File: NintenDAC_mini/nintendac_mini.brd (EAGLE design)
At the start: 26 x 42 mm, 30 parts, among them IC1 STM32F10XCXT6, IC3 24C64ST, X1 USB-MICROB

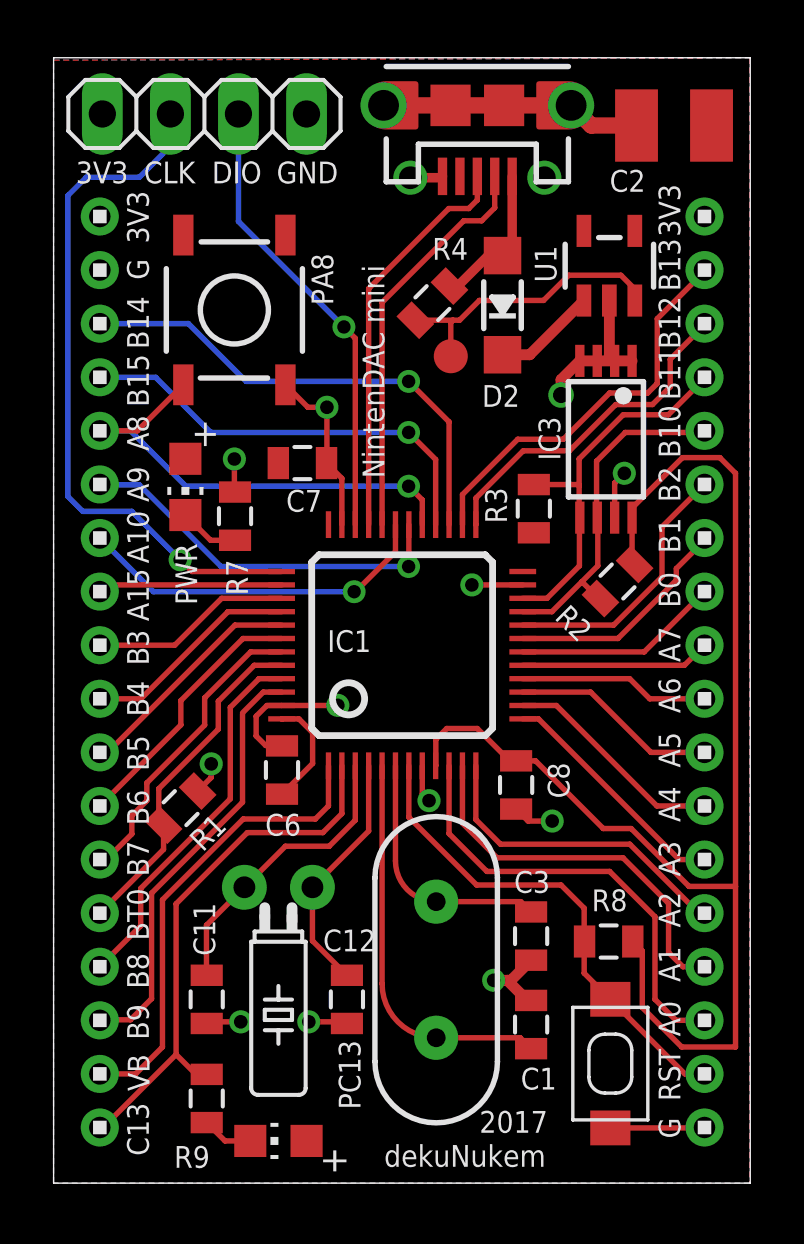
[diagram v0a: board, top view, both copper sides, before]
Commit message: updated power control on mini
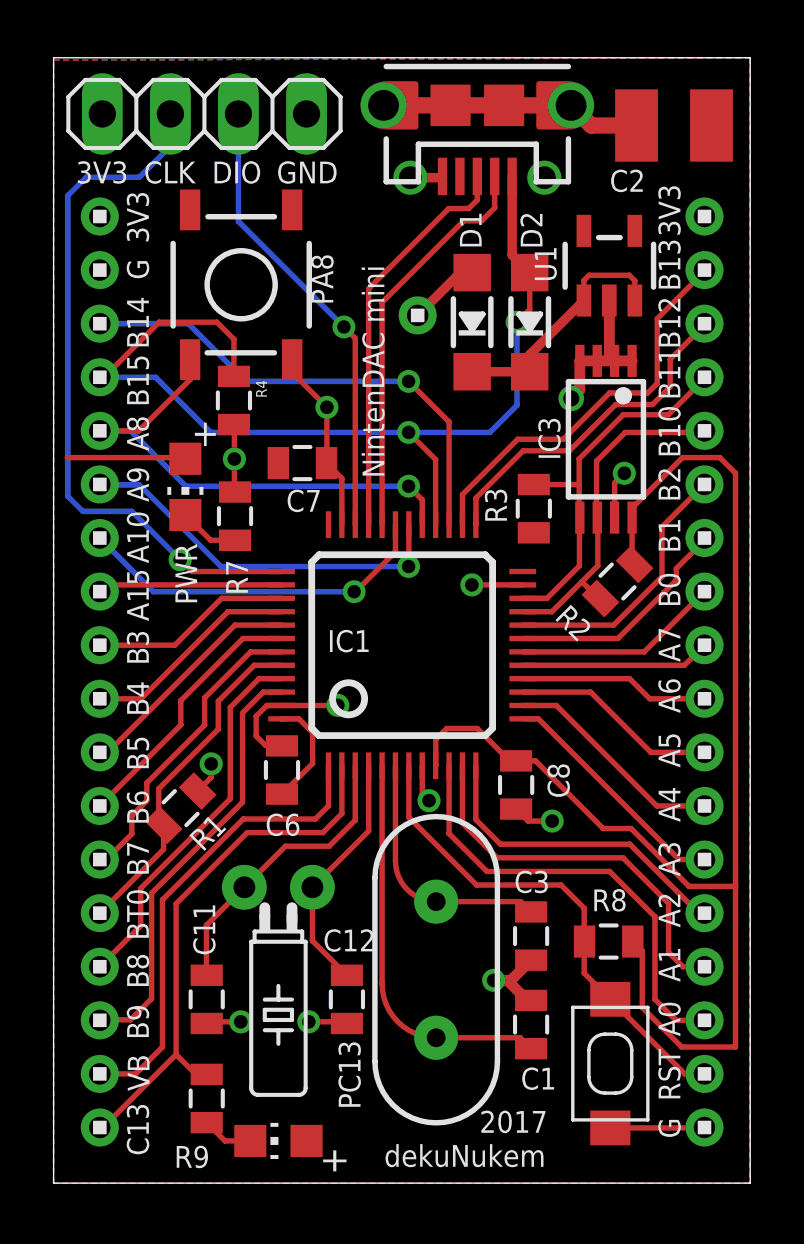
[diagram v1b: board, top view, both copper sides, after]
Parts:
- removed TP1: TEST-POINT3X5, SparkFun-Passives:PAD.03X.05
- added D1: MBR120, microbuilder:SOD-123
- added U$3: 1X1, headers(2mm):1X1
- moved R4 8.25 mm to (6.73, 29.2), turned to 270 degrees
- moved D2 1.20 mm to (17.8, 32.1)
- moved S2 0.97 mm to (7.00, 33.5)
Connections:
- removed net N$2: D2.A, R4.2, X1.VBUS
- net GND: now also R4.2
- net N$31: now also D1.C, U1.3
- net N$36: now also D1.A, U$3.1; no longer R4.1, TP1.P$1, U1.3
- net N$45: now also D2.A, R4.1, X1.VBUS
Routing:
- net N$45: track 16.2 -> 37.2 mm, vias 1 -> 2
- net N$36: track 11.0 -> 2.69 mm
- net N$2: track 5.56 -> 0.00 mm
- net N$31: track 3.88 -> 9.20 mm
- net +3V3: track 54.3 -> 58.7 mm
- net GND: track 46.7 -> 48.4 mm
- net N$43: track 17.9 -> 18.9 mm

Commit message: standby wakeup test
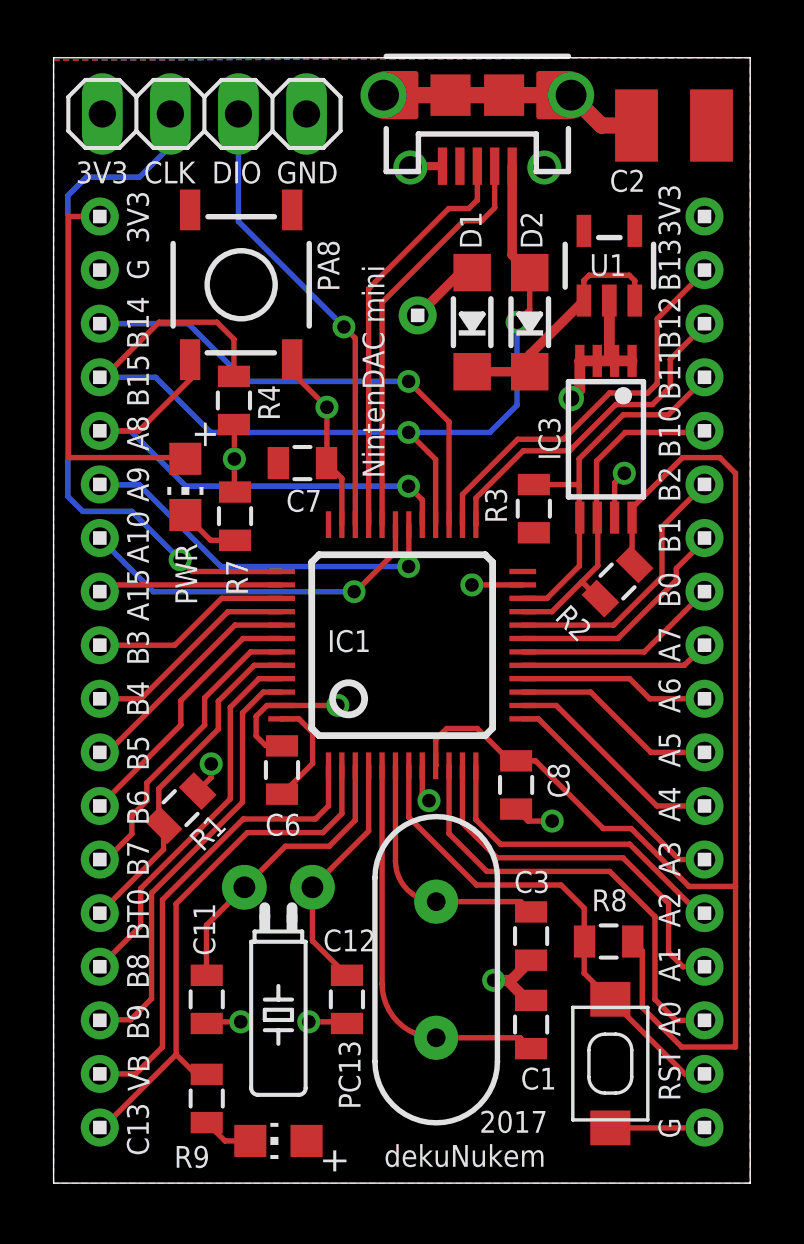
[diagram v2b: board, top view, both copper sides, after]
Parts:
- moved X1 0.38 mm to (15.8, 40.6)
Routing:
- net +3V3: track 58.7 -> 68.7 mm
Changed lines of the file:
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@@
 <setting verticaltext="up"/>
 </settings>
-<grid distance="1" unitdist="mil" unit="mil" style="lines" multiple="1" display="no" altdistance="0.025" altunitdist="inch" altunit="inch"/>
+<grid distance="5" unitdist="mil" unit="mil" style="lines" multiple="1" display="no" altdistance="0.025" altunitdist="inch" altunit="inch"/>
 <layers>
-<layer number="1" name="Top" color="4" fill="1" visible="no" active="yes"/>
+<layer number="1" name="Top" color="4" fill="1" visible="yes" active="yes"/>
 <layer number="16" name="Bottom" color="1" fill="1" visible="yes" active="yes"/>
 <layer number="17" name="Pads" color="2" fill="1" visible="yes" active="yes"/>
@@
 <text x="8.3218" y="37.3126" size="0.8128" layer="25">GND</text>
 <text x="10.6426" y="5.334" size="0.8128" layer="25" distance="10" rot="R270">PC13</text>
-<text x="10.4394" y="32.766" size="0.8128" layer="25" distance="10" rot="R90">PA8</text>
+<text x="10.668" y="33.274" size="0.8128" layer="25" distance="10" rot="R90">PA8</text>
 <text x="4.5466" y="23.876" size="0.8128" layer="25" distance="10" rot="R270">PWR</text>
 <text x="2.7432" y="6.6802" size="0.8128" layer="25" distance="10" rot="R270">B9</text>
@@
 </element>
 <element name="S1" library="Adafruit Feather M0 Adalogger" package="KMR2" value="SWITCH-MOMENTARY-2TURTLE" x="20.778" y="4.46" smashed="yes" rot="R90"/>
-<element name="X1" library="backplane" package="USB-MICROB" value="USB-MICROB" x="15.8148" y="40.2234" smashed="yes" rot="R180">
-<attribute name="PROD_ID" value="CONN-09505" x="15.8148" y="40.2234" size="1.778" layer="27" rot="R180" display="off"/>
+<element name="X1" library="backplane" package="USB-MICROB" value="USB-MICROB" x="15.8148" y="40.6044" smashed="yes" rot="R180">
+<attribute name="PROD_ID" value="CONN-09505" x="15.8148" y="40.6044" size="1.778" layer="27" rot="R180" display="off"/>
 </element>
 <element name="Y1" library="backplane" package="HC49US" value="" x="14.2794" y="7.9652" smashed="yes" rot="R270">
@@
 </element>
 <element name="U1" library="Adafruit Feather M0 Adalogger" package="SOT23-5" value="" x="20.7424" y="34.2392" smashed="yes">
-<attribute name="NAME" x="18.7706" y="33.617" size="0.8128" layer="25" ratio="18" rot="R90"/>
+<attribute name="NAME" x="21.374" y="34.671" size="0.8128" layer="25" ratio="18" rot="R180"/>
 <attribute name="VALUE" x="22.7204" y="33.6042" size="0.4064" layer="27" ratio="10"/>
 </element>
@@
 <element name="U$3" library="headers(2mm)" package="1X1" value="1X1" x="13.589" y="32.385" smashed="yes"/>
 <element name="R4" library="SparkFun-Passives" package="0805" value="" x="6.731" y="29.21" smashed="yes" rot="R270">
-<attribute name="NAME" x="7.5565" y="29.972" size="0.4064" layer="25" rot="R270"/>
+<attribute name="NAME" x="7.6327" y="29.7942" size="0.8128" layer="25" rot="R270"/>
 <attribute name="VALUE" x="5.334" y="30.226" size="0.4064" layer="27" rot="R270"/>
 </element>
@@
 <contactref element="U1" pad="2"/>
 <via x="19.32" y="29.2862" extent="1-16" drill="0.6"/>
-<wire x1="12.3148" y1="40.2234" x2="14.8148" y2="40.2234" width="0.6096" layer="1"/>
-<wire x1="14.8148" y1="40.2234" x2="16.8148" y2="40.2234" width="0.6096" layer="1"/>
+<wire x1="12.3148" y1="40.6044" x2="14.8148" y2="40.6044" width="0.6096" layer="1"/>
+<wire x1="14.8148" y1="40.6044" x2="16.8148" y2="40.6044" width="0.6096" layer="1"/>
 <wire x1="20.778" y1="2.06" x2="24.2772" y2="2.06" width="0.2032" layer="1"/>
 <wire x1="24.2772" y1="2.06" x2="24.2934" y2="2.0762" width="0.2032" layer="1"/>
-<wire x1="5.9994" y1="6.0342" x2="6.0138" y2="6.0198" width="0.2032" layer="1"/>
 <wire x1="10.9474" y1="5.958" x2="10.8856" y2="6.0198" width="0.2032" layer="1"/>
 <wire x1="10.8856" y1="6.0198" x2="9.525" y2="6.0198" width="0.2032" layer="1"/>
-<wire x1="6.985" y1="6.0198" x2="5.7768" y2="6.0198" width="0.2032" layer="1"/>
-<wire x1="5.7768" y1="6.0198" x2="5.715" y2="5.958" width="0.2032" layer="1"/>
 <wire x1="21.3012" y1="26.4922" x2="20.9404" y2="26.1314" width="0.2032" layer="1"/>
 <wire x1="20.9404" y1="26.1314" x2="20.9404" y2="24.8372" width="0.2032" layer="1"/>
@@
 <wire x1="20.7424" y1="32.9391" x2="20.7424" y2="30.8852" width="0.4064" layer="1"/>
 <wire x1="20.7424" y1="30.8852" x2="20.9404" y2="30.6872" width="0.4064" layer="1"/>
-<wire x1="19.3148" y1="40.2234" x2="20.0666" y2="39.4716" width="0.6096" layer="1"/>
-<wire x1="20.0666" y1="39.4716" x2="21.7554" y2="39.4716" width="0.6096" layer="1"/>
 <wire x1="5.37679375" y1="14.63179375" x2="5.8834" y2="15.1384" width="0.2032" layer="1"/>
 <wire x1="5.8834" y1="15.1384" x2="5.8834" y2="15.6464" width="0.2032" layer="1"/>
-<wire x1="19.3148" y1="40.2234" x2="16.8148" y2="40.2234" width="0.6096" layer="1"/>
-<wire x1="13.3148" y1="37.5234" x2="14.4648" y2="37.5234" width="0.3556" layer="1"/>
-<wire x1="14.4648" y1="37.5234" x2="14.5148" y2="37.5734" width="0.3556" layer="1"/>
+<wire x1="19.3148" y1="40.6044" x2="16.8148" y2="40.6044" width="0.6096" layer="1"/>
 <wire x1="19.32" y1="29.2862" x2="19.6404" y2="29.6066" width="0.4064" layer="1"/>
 <wire x1="19.6404" y1="29.6066" x2="19.6404" y2="30.6872" width="0.4064" layer="1"/>
@@
 <wire x1="10.2014" y1="28.956" x2="8.906" y2="30.2514" width="0.2032" layer="1"/>
 <wire x1="8.906" y1="30.2514" x2="8.906" y2="30.734" width="0.2032" layer="1"/>
-<wire x1="5.7768" y1="6.0198" x2="5.9994" y2="6.0342" width="0" layer="19" extent="1-1"/>
+<wire x1="5.715" y1="5.958" x2="5.7768" y2="6.0198" width="0.2032" layer="1"/>
+<wire x1="5.7768" y1="6.0198" x2="6.985" y2="6.0198" width="0.2032" layer="1"/>
+<wire x1="13.3148" y1="37.9044" x2="13.3648" y2="37.9544" width="0.3048" layer="1"/>
+<wire x1="13.3648" y1="37.9544" x2="14.5148" y2="37.9544" width="0.3048" layer="1"/>
+<wire x1="19.3148" y1="40.6044" x2="20.4476" y2="39.4716" width="0.6096" layer="1"/>
+<wire x1="20.4476" y1="39.4716" x2="21.7554" y2="39.4716" width="0.6096" layer="1"/>
 </signal>
 <signal name="+3V3">
@@
 <contactref element="JP1" pad="4"/>
 <contactref element="U1" pad="5"/>
-<wire x1="19.7772" y1="35.4076" x2="19.7772" y2="35.6108" width="0.4064" layer="1"/>
 <wire x1="21.5904" y1="23.1831875" x2="21.68359375" y2="23.08999375" width="0.2032" layer="1"/>
 <wire x1="21.617" y1="9.017" x2="21.971" y2="8.663" width="0.2032" layer="1"/>
@@
 <wire x1="17.9882" y1="15.759" x2="17.2626" y2="15.759" width="0.2032" layer="1"/>
 <wire x1="21.5904" y1="24.8372" x2="21.5904" y2="23.1831875" width="0.2032" layer="1"/>
-<wire x1="4.9014" y1="27.0764" x2="0.508" y2="27.0764" width="0.2032" layer="1"/>
-<wire x1="19.7924" y1="35.5393" x2="19.7772" y2="35.6108" width="0" layer="19" extent="1-1"/>
+<wire x1="0.5588" y1="27.0764" x2="0.5588" y2="36.0762" width="0.2032" layer="1"/>
+<wire x1="0.5588" y1="36.0762" x2="1.7254" y2="36.0762" width="0.2032" layer="1"/>
+<wire x1="0.5588" y1="27.0764" x2="4.9182" y2="27.0764" width="0.2032" layer="1"/>
+<wire x1="4.9182" y1="27.0764" x2="4.9182" y2="27.0342" width="0.2032" layer="1"/>
 </signal>
 <signal name="N$1">
@@
 <wire x1="14.748" y1="36.3728" x2="15.494" y2="36.3728" width="0.2032" layer="1"/>
 <wire x1="15.494" y1="36.3728" x2="15.8148" y2="36.6936" width="0.2032" layer="1"/>
-<wire x1="15.8148" y1="36.6936" x2="15.8148" y2="37.5734" width="0.2032" layer="1"/>
+<wire x1="15.8148" y1="36.6936" x2="15.8148" y2="37.9544" width="0.2032" layer="1"/>
 </signal>
 <signal name="N$7">
@@
 <wire x1="15.3068" y1="35.9156" x2="15.9766" y2="35.9156" width="0.2032" layer="1"/>
 <wire x1="15.9766" y1="35.9156" x2="16.4648" y2="36.4038" width="0.2032" layer="1"/>
-<wire x1="16.4648" y1="36.4038" x2="16.4648" y2="37.5734" width="0.2032" layer="1"/>
+<wire x1="16.4648" y1="36.4038" x2="16.4648" y2="37.9544" width="0.2032" layer="1"/>
 </signal>
 <signal name="N$8">
@@
 <contactref element="IC1" pad="46"/>
 <contactref element="U$1" pad="16"/>
-<wire x1="7.0518" y1="14.2146" x2="7.0518" y2="17.5006" width="0.2032" layer="1"/>
 <wire x1="7.0518" y1="17.5514" x2="7.8266" y2="18.3262" width="0.2032" layer="1"/>
 <wire x1="7.8266" y1="18.3262" x2="8.5094" y2="18.3262" width="0.2032" layer="1"/>
@@
 <wire x1="2.8702" y1="6.096" x2="1.7452" y2="6.096" width="0.2032" layer="1"/>
 <wire x1="1.7452" y1="6.096" x2="1.7254" y2="6.0762" width="0.2032" layer="1"/>
-<wire x1="7.0518" y1="17.5006" x2="7.0518" y2="17.5514" width="0" layer="19" extent="1-1"/>
+<wire x1="7.0518" y1="17.5514" x2="7.0518" y2="14.2146" width="0.2032" layer="1"/>
 </signal>
 <signal name="N$35">
@@
 <contactref element="D2" pad="A"/>
 <contactref element="X1" pad="VBUS"/>
-<wire x1="17.1148" y1="37.5734" x2="17.1148" y2="34.6368" width="0.3556" layer="1"/>
+<wire x1="17.1148" y1="37.9544" x2="17.1148" y2="34.6368" width="0.3556" layer="1"/>
 <wire x1="17.1148" y1="34.6368" x2="17.7706" y2="33.981" width="0.3556" layer="1"/>
 <via x="17.2974" y="32.131" extent="1-16" drill="0.5"/>

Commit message: board cleanup
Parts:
- moved U$3 1.09 mm to (13.1, 31.4)
- moved X1 0.99 mm to (15.2, 39.8)
- moved C2 0.90 mm to (22.5, 38.8)
- moved C7 0.90 mm to (8.65, 26.2)
- moved D2 0.90 mm to (17.1, 31.5)
- moved IC3 0.90 mm to (20.0, 27.1)
- moved R2 0.90 mm to (20.4, 21.8)
- moved Y1 0.90 mm to (13.6, 7.33)
- moved C1 0.90 mm to (17.2, 5.28)
- moved C3 0.90 mm to (17.2, 8.59)
- moved D1 0.90 mm to (15.0, 31.5)
- moved IC1 0.90 mm to (12.4, 19.4)
- moved PWR 0.90 mm to (4.28, 25.3)
- moved R4 0.90 mm to (6.10, 28.6)
- moved C6 0.90 mm to (7.89, 14.8)
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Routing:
- net +3V3: track 68.7 -> 137.6 mm
- net N$9: track 26.2 -> 25.6 mm
- net N$45: track 37.6 -> 37.0 mm
- net N$43: track 18.9 -> 18.4 mm
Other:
- board size 26 x 42 mm -> 25 x 41 mm
- board text added: "VIN"

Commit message: removed wkup from headers
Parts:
- removed U$3: 1X1, headers(2mm):1X1
- moved R4 10.0 mm to (16.1, 28.2), turned to 0 degrees
- moved D1 0.25 mm to (15.0, 31.8)
- moved D2 0.25 mm to (17.1, 31.8)
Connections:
- removed net N$36: D1.A, U$3.1
- new net N$2: D1.A, U$1.3
- net N$44: now also U$1.4; no longer U$1.3
- net N$45: no longer U$1.4
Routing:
- net N$45: track 37.0 -> 17.6 mm, vias 2 -> 0
- net N$2: track 0.00 -> 14.5 mm, vias 0 -> 1
- net N$36: track 2.72 -> 0.00 mm
- net N$44: track 18.1 -> 17.4 mm
- net GND: track 48.5 -> 49.0 mm
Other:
- board text removed: "B15"
